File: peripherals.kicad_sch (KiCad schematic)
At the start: 18 parts, among them SW1 CHIP_EN, SW2 BTN1, SW3 BTN2, U4 AD623, U5 MCP6001U

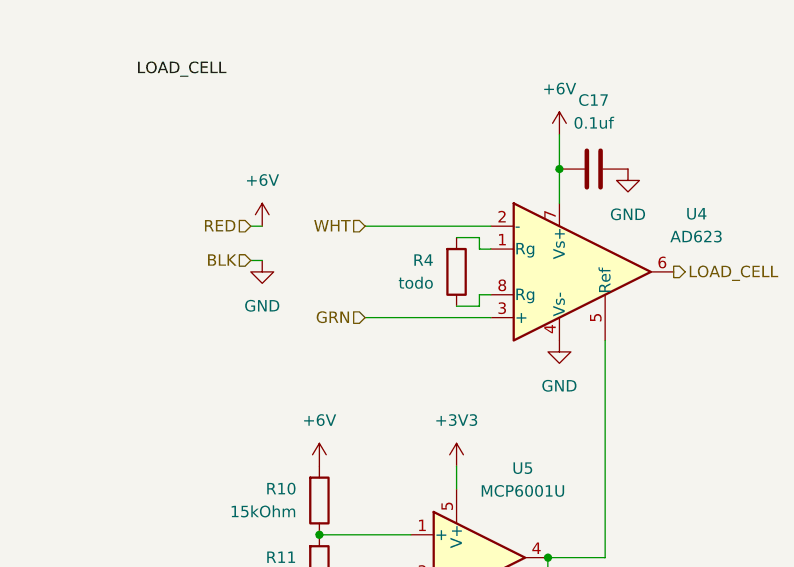
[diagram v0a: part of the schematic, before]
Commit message: fix: set ad623 gain
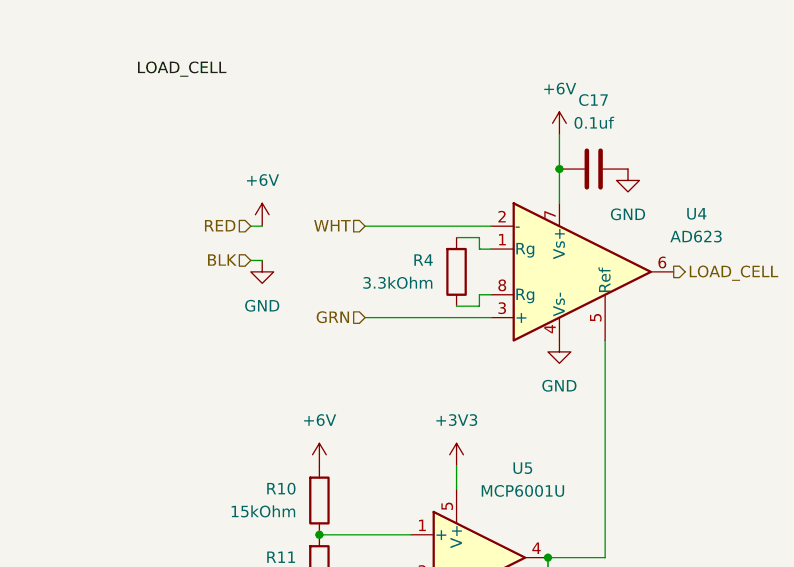
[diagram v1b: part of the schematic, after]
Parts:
- R4: value todo -> 3.3kOhm
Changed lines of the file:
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@@
 			)
 		)
-		(property "Value" "todo"
+		(property "Value" "3.3kOhm"
 			(at 58.42 99.0599 0)
 			(effects

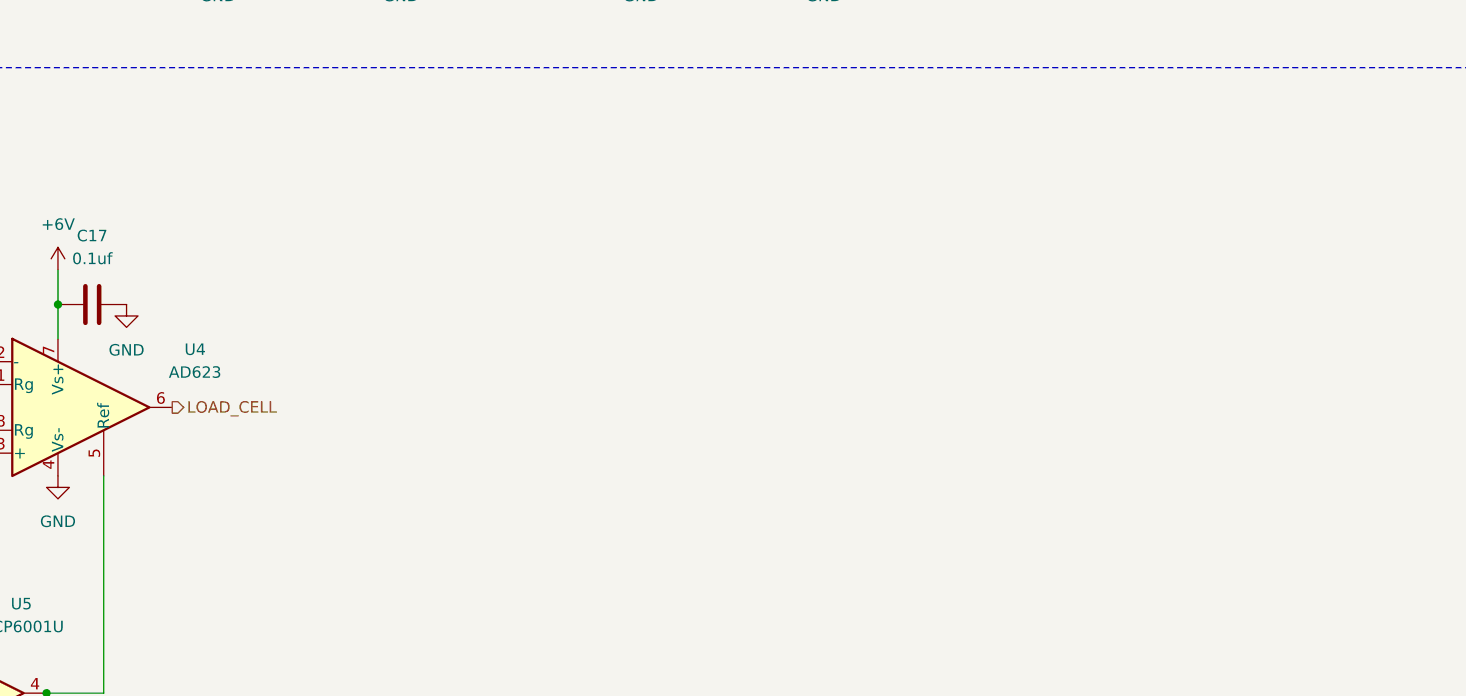
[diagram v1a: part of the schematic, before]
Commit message: feat: led_inf connected, load cell overvoltage protection and antenna vals defined
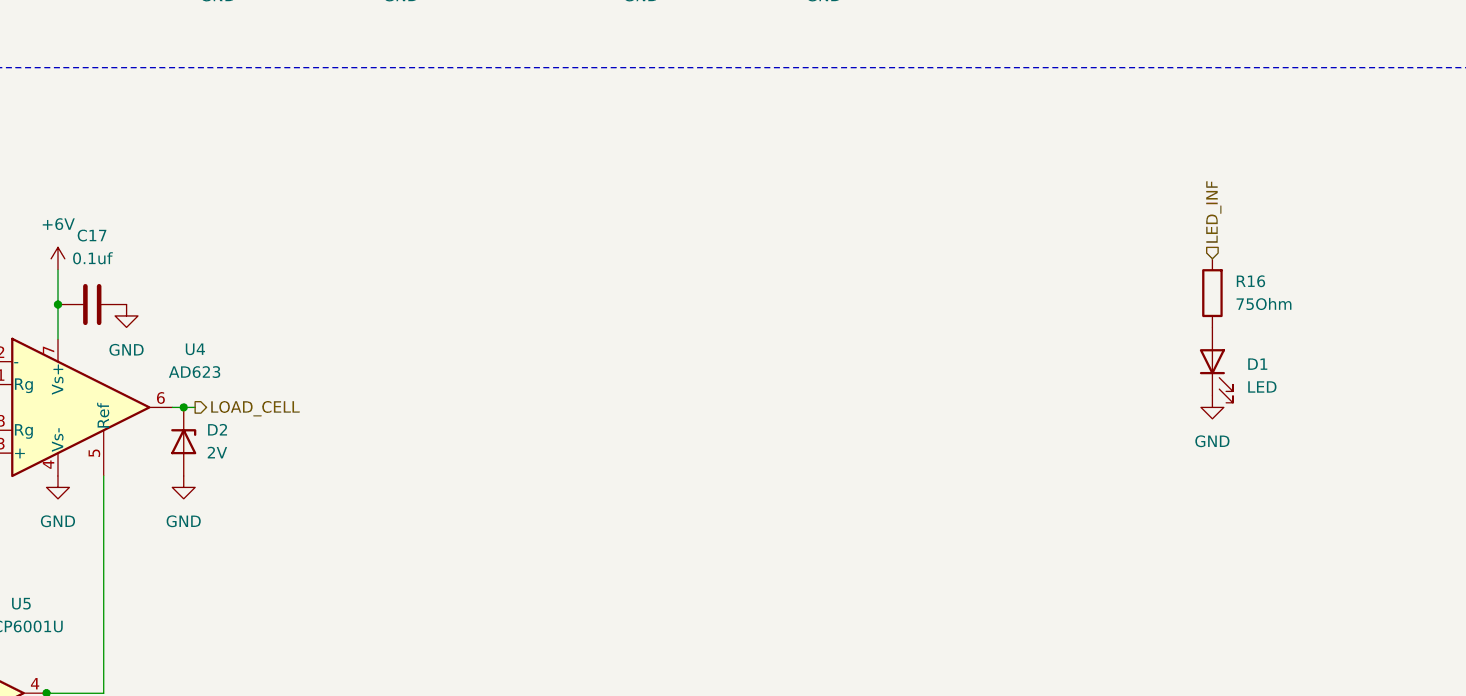
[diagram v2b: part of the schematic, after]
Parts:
- added D1: LED, LED_THT:LED_D3.0mm, symbol Device:LED
- added D2: 2V, Diode_SMD:D_0402_1005Metric_Pad0.77x0.64mm_HandSolder, symbol Device:D_Zener
- added R16: 75Ohm, Resistor_SMD:R_0402_1005Metric_Pad0.72x0.64mm_HandSolder, symbol Device:R
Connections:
- net GND: now also D1.1 (K), D2.2 (A)
- net LOAD_CELL: now also D2.1 (K)
- new net: D1.2 (A), R16.1
- new net LED_INF: R16.2

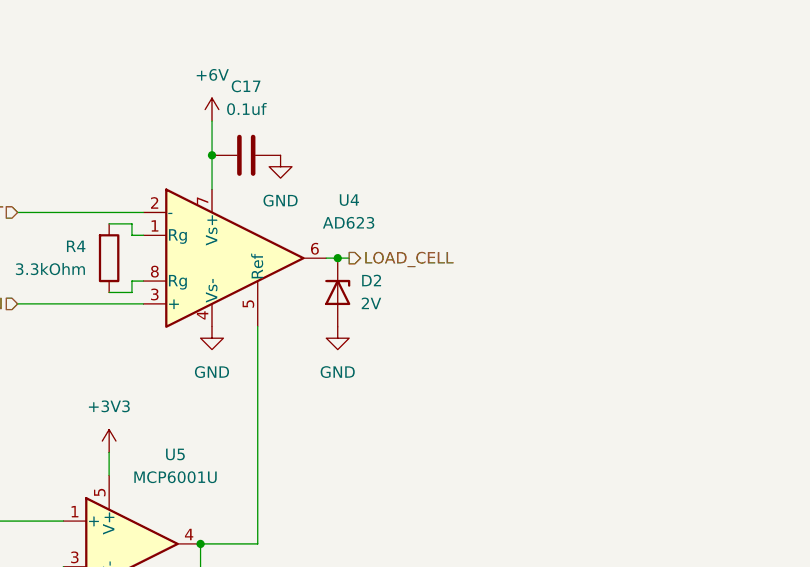
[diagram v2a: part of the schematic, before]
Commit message: fix: added resistor to load cell overvoltage protection
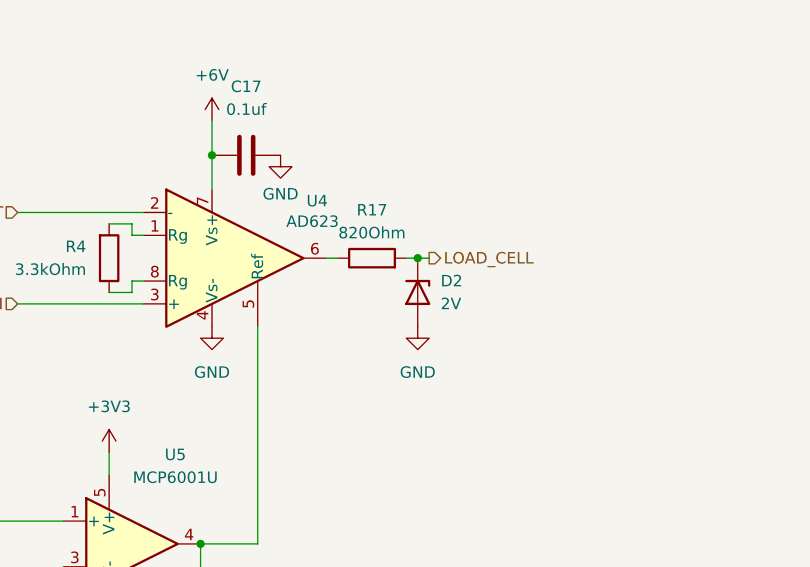
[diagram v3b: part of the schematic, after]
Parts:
- added R17: 820Ohm, Resistor_SMD:R_0402_1005Metric_Pad0.72x0.64mm_HandSolder, symbol Device:R
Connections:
- net LOAD_CELL: now also R17.2; no longer U4.6
- new net: R17.1, U4.6
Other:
- moved on the sheet: D2
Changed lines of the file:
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@@
 	(paper "A4")
 	(junction
-		(at 86.36 97.79)
+		(at 95.25 97.79)
 		(diameter 0)
 		(color 0 0 0 0)
@@
 	(wire
 		(pts
-			(xy 87.63 97.79) (xy 86.36 97.79)
+			(xy 96.52 97.79) (xy 95.25 97.79)
 		)
 		(stroke
@@
 	(wire
 		(pts
-			(xy 137.16 46.99) (xy 137.16 39.37)
+			(xy 85.09 97.79) (xy 86.36 97.79)
 		)
 		(stroke
@@
 	(wire
 		(pts
-			(xy 90.17 46.99) (xy 90.17 39.37)
+			(xy 93.98 97.79) (xy 95.25 97.79)
 		)
 		(stroke
@@
 	(wire
 		(pts
-			(xy 110.49 39.37) (xy 109.22 39.37)
+			(xy 137.16 46.99) (xy 137.16 39.37)
 		)
 		(stroke
@@
 	(wire
 		(pts
-			(xy 63.5 100.33) (xy 63.5 101.6)
+			(xy 90.17 46.99) (xy 90.17 39.37)
 		)
 		(stroke
@@
 	(wire
 		(pts
-			(xy 148.59 39.37) (xy 147.32 39.37)
+			(xy 110.49 39.37) (xy 109.22 39.37)
 		)
 		(stroke
@@
 	(wire
 		(pts
-			(xy 38.1 96.52) (xy 39.37 96.52)
+			(xy 63.5 100.33) (xy 63.5 101.6)
 		)
 		(stroke
@@
 	(wire
 		(pts
-			(xy 157.48 39.37) (xy 162.56 39.37)
+			(xy 148.59 39.37) (xy 147.32 39.37)
 		)
 		(stroke
@@
 	(wire
 		(pts
-			(xy 110.49 39.37) (xy 115.57 39.37)
+			(xy 38.1 96.52) (xy 39.37 96.52)
 		)
 		(stroke
@@
 	(wire
 		(pts
-			(xy 86.36 97.79) (xy 85.09 97.79)
+			(xy 157.48 39.37) (xy 162.56 39.37)
+		)
+		(stroke
+			(width 0)
+			(type default)
+		)
+	)
+	(wire
+		(pts
+			(xy 110.49 39.37) (xy 115.57 39.37)
 		)
 		(stroke
@@
 	(hierarchical_label "LOAD_CELL"
 		(shape output)
-		(at 87.63 97.79 0)
+		(at 96.52 97.79 0)
 		(effects
 			(font
@@
 	(symbol
 		(lib_id "Device:D_Zener")
-		(at 86.36 101.6 270)
+		(at 95.25 101.6 270)
 		(unit 1)
 		(exclude_from_sim no)
@@
 		(dnp no)
 		(property "Reference" "D2"
-			(at 88.9 100.3299 90)
+			(at 97.79 100.3299 90)
 			(effects
 				(font
@@
 		)
 		(property "Value" "2V"
-			(at 88.9 102.8699 90)
+			(at 97.79 102.8699 90)
 			(effects
 				(font
@@
 		)
 		(property "Footprint" "Diode_SMD:D_0402_1005Metric_Pad0.77x0.64mm_HandSolder"
-			(at 86.36 101.6 0)
+			(at 95.25 101.6 0)
 			(effects
 				(font
@@
 		)
 		(property "Datasheet" "~"
-			(at 86.36 101.6 0)
+			(at 95.25 101.6 0)
 			(effects
 				(font
@@
 		)
 		(property "Description" "Zener diode"
-			(at 86.36 101.6 0)
+			(at 95.25 101.6 0)
 			(effects
 				(font
@@
 		(on_board yes)
 		(dnp no)
-		(fields_autoplaced yes)
 		(property "Reference" "U4"
-			(at 87.63 91.3698 0)
+			(at 84.074 91.44 0)
 			(effects
 				(font
@@
 		)
 		(property "Value" "AD623"
-			(at 87.63 93.9098 0)
+			(at 83.566 93.726 0)
 			(effects
 				(font
@@
 		(on_board yes)
 		(dnp no)
-		(fields_autoplaced yes)
 		(property "Reference" "#PWR030"
 			(at 80.01 92.71 0)
@@
 		)
 		(property "Value" "GND"
-			(at 80.01 91.44 0)
+			(at 80.01 90.678 0)
 			(effects
 				(font
@@
 	(symbol
 		(lib_id "power:GND")
-		(at 86.36 105.41 0)
+		(at 95.25 105.41 0)
 		(unit 1)
 		(exclude_from_sim no)
@@
 		(fields_autoplaced yes)
 		(property "Reference" "#PWR052"
-			(at 86.36 111.76 0)
+			(at 95.25 111.76 0)
 			(effects
 				(font
@@
 		)
 		(property "Value" "GND"
-			(at 86.36 110.49 0)
+			(at 95.25 110.49 0)
 			(effects
 				(font
@@
 		)
 		(property "Footprint" ""
-			(at 86.36 105.41 0)
+			(at 95.25 105.41 0)
 			(effects
 				(font
@@
 		)
 		(property "Datasheet" ""
-			(at 86.36 105.41 0)
+			(at 95.25 105.41 0)
 			(effects
 				(font
@@
 		)
 		(property "Description" "Power symbol creates a global label with name \"GND\" , ground"
-			(at 86.36 105.41 0)
+			(at 95.25 105.41 0)
 			(effects
 				(font
@@
 					(unit 1)
 				)
+			)
+		)
+	)
+	(symbol
+		(lib_id "Device:R")
+		(at 90.17 97.79 90)
+		(unit 1)
+		(exclude_from_sim no)
+		(in_bom yes)
+		(on_board yes)
+		(dnp no)
+		(property "Reference" "R17"
+			(at 90.17 92.456 90)
+			(effects
+				(font
+					(size 1.27 1.27)
+				)
+			)
+		)
+		(property "Value" "820Ohm"
+			(at 90.17 94.996 90)
+			(effects
+				(font
+					(size 1.27 1.27)
+				)
+			)
+		)
+		(property "Footprint" "Resistor_SMD:R_0402_1005Metric_Pad0.72x0.64mm_HandSolder"
+			(at 90.17 99.568 90)
+			(effects
+				(font
+					(size 1.27 1.27)
+				)
+				(hide yes)
+			)
+		)
+		(property "Datasheet" "~"
+			(at 90.17 97.79 0)
+			(effects
+				(font
+					(size 1.27 1.27)
+				)
+				(hide yes)
+			)
+		)
+		(property "Description" "Resistor"
+			(at 90.17 97.79 0)
+			(effects
+				(font
+					(size 1.27 1.27)
+				)
+				(hide yes)
+			)
+		)
+		(pin "2"
+		)
+		(pin "1"
+		)
+		(instances
+			(project ""
+				(path "/9edf3a40-33ab-40a8-8c54-e53c70f0a44f/a1d4e011-9c91-4e2d-9868-4caa044f2ad9"
+					(reference "R17")
+					(unit 1)
+				)

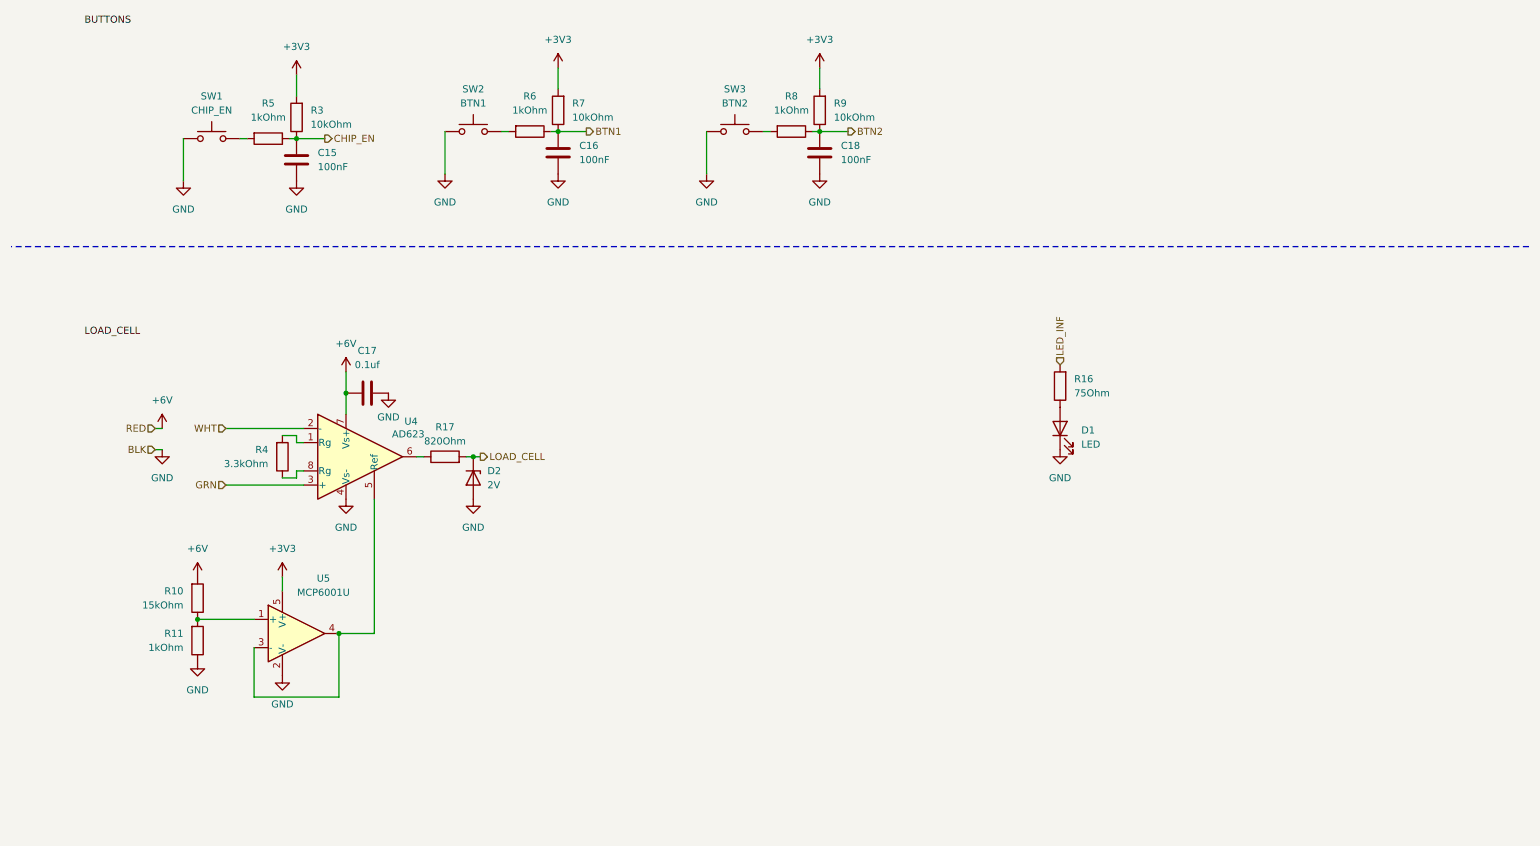
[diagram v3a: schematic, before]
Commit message: feat: added power button, name changes
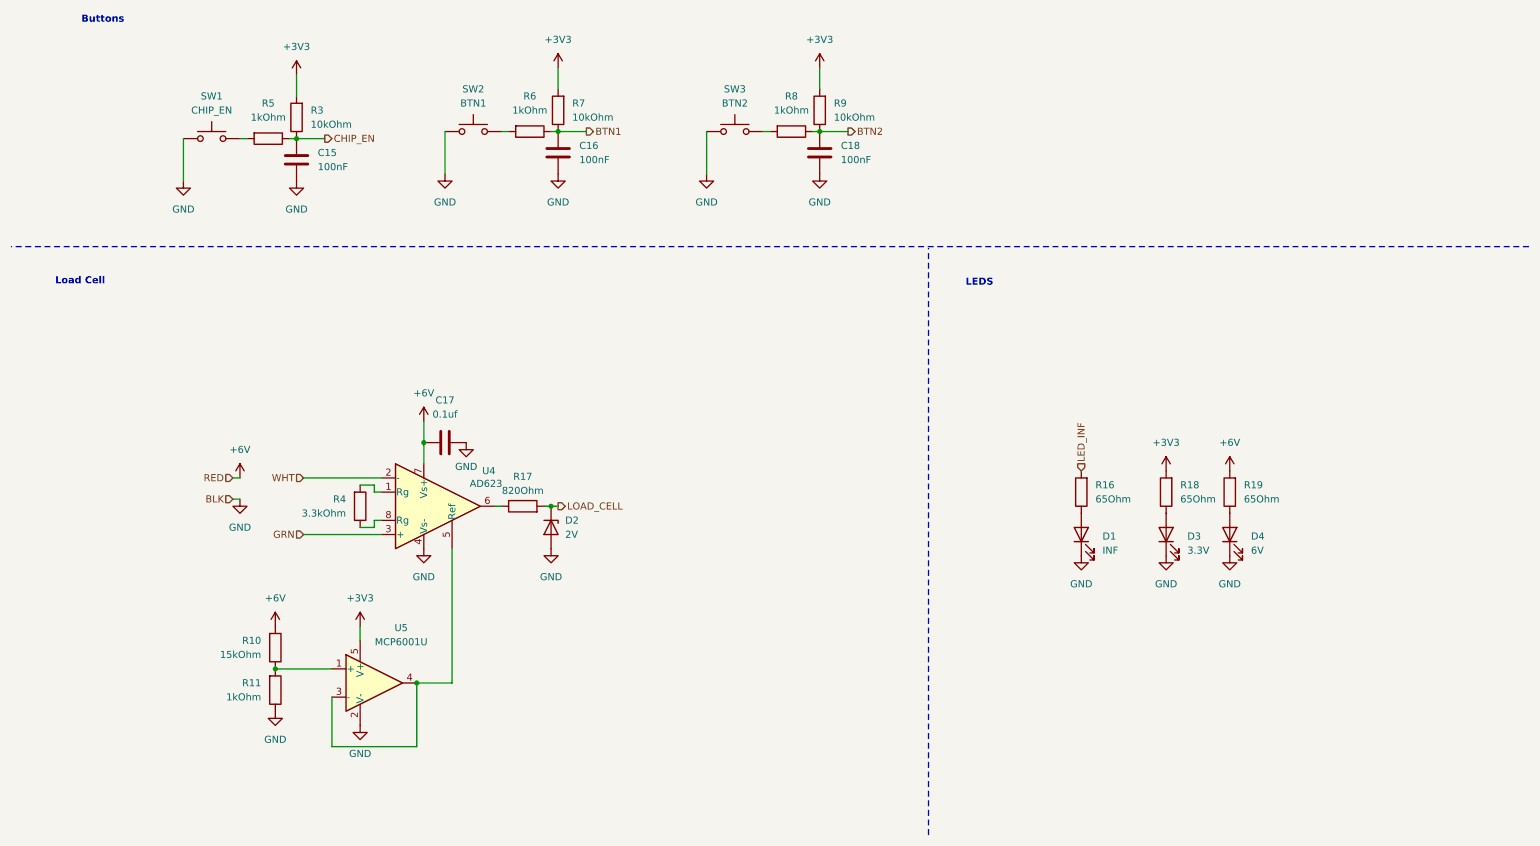
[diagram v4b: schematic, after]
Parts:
- added D3: 3.3V, LED_SMD:LED_0402_1005Metric, symbol Device:LED
- added D4: 6V, LED_SMD:LED_0402_1005Metric, symbol Device:LED
- added R18, R19: 65Ohm, Resistor_SMD:R_0402_1005Metric_Pad0.72x0.64mm_HandSolder, symbol Device:R
- D1: value LED -> INF; footprint LED_THT:LED_D3.0mm -> LED_SMD:LED_0402_1005Metric
- R16: value 75Ohm -> 65Ohm
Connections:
- net +3V3: now also R18.2
- net +6V: now also R19.2
- net GND: now also D3.1 (K), D4.1 (K)
- new net: D3.2 (A), R18.1
- new net: D4.2 (A), R19.1
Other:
- note added: "Buttons"
- note added: "LEDS"
- note added: "Load Cell"
- moved on the sheet: C17, D2, R10, R11, R16, R17, R4, U4, U5

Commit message: wip: pcb layout started
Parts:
- removed U5: MCP6001U, symbol Amplifier_Operational:MCP6001U
- added Buffer1: MCP6001U, Package_TO_SOT_SMD:SOT-23-5, symbol Amplifier_Operational:MCP6001U
- renumbered C15 to C200, C16 to C201, C18 to C202, C17 to C203, D2 to D200, D1 to D201, D3 to D202, D4 to D203, R19 to R112, R5 to R200, R3 to R201, R6 to R202, R7 to R203, R8 to R204, R9 to R205, R4 to R206, R17 to R207, R10 to R208, R11 to R209, R16 to R210, R18 to R211
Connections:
- net +3V3: now also Buffer1.5 (V+)
- net GND: now also Buffer1.2 (V-)
- net at U4.5 (Ref): now also Buffer1.3 (-), Buffer1.4
- net at R208.1, R209.2: now also Buffer1.1 (+)
